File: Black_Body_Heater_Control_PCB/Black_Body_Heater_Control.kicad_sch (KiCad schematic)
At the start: 0 parts

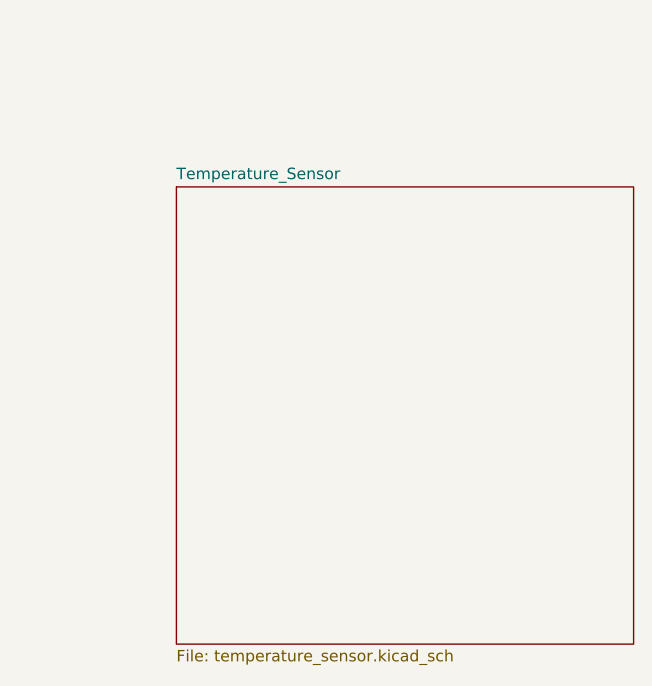
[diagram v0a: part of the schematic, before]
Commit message: Buck spice file not working, created new pcb
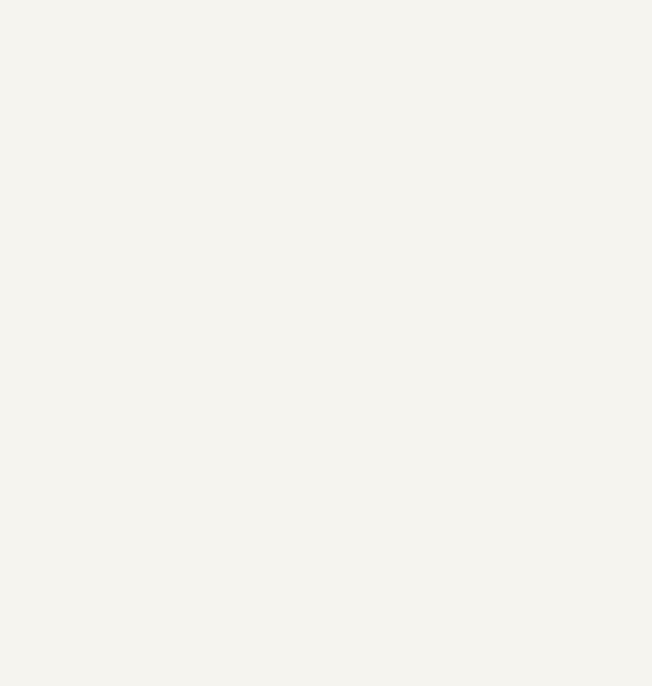
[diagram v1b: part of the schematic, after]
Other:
- removed sheet Temperature_Sensor
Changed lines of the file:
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@@
-	)
-	(sheet
-		(at 228.6 76.2)
-		(size 50.8 50.8)
-		(exclude_from_sim no)
-		(in_bom yes)
-		(on_board yes)
-		(dnp no)
-		(fields_autoplaced yes)
-		(stroke
-			(width 0.1524)
-			(type solid)
-		)
-		(fill
-			(color 0 0 0 0)
-		)
-		(property "Sheetname" "Temperature_Sensor"
-			(at 228.6 75.4884 0)
-			(show_name no)
-			(do_not_autoplace no)
-			(effects
-				(font
-					(size 1.27 1.27)
-				)
-				(justify left bottom)
-			)
-		)
-		(property "Sheetfile" "temperature_sensor.kicad_sch"
-			(at 228.6 127.5846 0)
-			(show_name no)
-			(do_not_autoplace no)
-			(effects
-				(font
-					(size 1.27 1.27)
-				)
-				(justify left top)
-			)
-		)
-		(instances
-			(project "Black_Body_Heater_Control"
-				(path "/f3dd8e24-b1a1-45ed-a541-b7ae36b7e8e0"
-					(page "4")
-				)
-			)
-		)
 	)
 	(sheet
